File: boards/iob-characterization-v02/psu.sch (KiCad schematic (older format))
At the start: 0 parts

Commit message: Continued work on IOB characterization v0.2 board. On hold until protection network is figured out
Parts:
- added U11, U12: SIP32408, symbol SIP32408
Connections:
- net labels added: VCCO_HI, VCCO_LO
- net labels removed: VCCO
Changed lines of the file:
@@
 encoding utf-8
 Sheet 2 2
-Title ""
-Date ""
-Rev ""
-Comp ""
+Title "STARSHIPRAIDER I/O Characterization"
+Date "2017-05-18"
+Rev "0.2"
+Comp "Andrew Zonenberg"
 Comment1 ""
 Comment2 ""
@@
 I2C to host is 3.3V, shift it to 5V
 Text HLabel 5050 1000 0    60   Output ~ 0
-VCCO
+VCCO_HI
 Text HLabel 5050 1100 0    60   Output ~ 0
 VCLIP_HI
@@
 Text HLabel 5050 1350 0    60   Output ~ 0
 2V5
+Text HLabel 5050 900  0    60   Output ~ 0
+VCCO_LO
+$Comp
+L SIP32408 U11
+U 1 1 591F646E
+P 7100 2250
+F 0 "U11" H 7400 3047 60  0000 C CNN
+F 1 "SIP32408" H 7400 2941 60  0000 C CNN
+F 2 "" H 7100 2250 60  0000 C CNN
+F 3 "" H 7100 2250 60  0000 C CNN
+	1    7100 2250
+	1    0    0    -1
+$EndComp
+$Comp
+L SIP32408 U12
+U 1 1 591F64B0
+P 7100 3300
+F 0 "U12" H 7400 4097 60  0000 C CNN
+F 1 "SIP32408" H 7400 3991 60  0000 C CNN
+F 2 "" H 7100 3300 60  0000 C CNN
+F 3 "" H 7100 3300 60  0000 C CNN
+	1    7100 3300
+	1    0    0    -1
+$EndComp
 $EndSCHEMATC

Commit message: Continued work on iob characterization board
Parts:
- added J2: GREENPAK_DEVKIT_HDR, symbol iob-characterization-v02-rescue:GREENPAK_DEVKIT_HDR
- added R1, R2: R, symbol iob-characterization-v02-rescue:R
- added U1: ISL24021IRT065Z-T7A‎, symbol analog-azonenberg:ISL24021IRT065Z-T7A‎
- U11, U12: value SIP32408 -> SIP32409; symbol SIP32408 -> iob-characterization-v02-rescue:SIP32408
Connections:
- net labels added: VCCO, VCCO_ATTEN, VCCO_IS_HI, VCCO_IS_LO, VCCO_REF
- net labels removed: I2C_SCL, I2C_SDA, VCLIP_HI, VCLIP_LO
- wire segments 0 -> 28
- no-connect marks 0 -> 2
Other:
- note added: "Buffer DAC output to generate VCCO"
- note added: "Greenpak runs at 5V Vdd"
- note added: "Load switches for output power rails"
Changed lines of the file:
@@
-EESchema Schematic File Version 2
-LIBS:conn
-LIBS:device
-LIBS:analog-azonenberg
-LIBS:cmos
-LIBS:cypress-azonenberg
-LIBS:hirose-azonenberg
-LIBS:memory-azonenberg
-LIBS:microchip-azonenberg
-LIBS:osc-azonenberg
-LIBS:passive-azonenberg
-LIBS:power-azonenberg
-LIBS:special-azonenberg
-LIBS:xilinx-azonenberg
+EESchema Schematic File Version 4
 LIBS:iob-characterization-v02-cache
 EELAYER 26 0
@@
 $Descr A4 11693 8268
 encoding utf-8
-Sheet 2 2
+Sheet 2 6
 Title "STARSHIPRAIDER I/O Characterization"
-Date "2017-05-18"
+Date "2018-08-09"
 Rev "0.2"
-Comp "Andrew Zonenberg"
+Comp "Andrew D. Zonenberg"
 Comment1 ""
 Comment2 ""
@@
 Text HLabel 1600 850  0    60   Input ~ 0
 12V0
-Text HLabel 1600 950  0    60   Input ~ 0
+Text HLabel 5300 5350 0    60   Input ~ 0
 5V0
-Text HLabel 1600 1050 0    60   Input ~ 0
+Text HLabel 5300 5450 0    60   Input ~ 0
 GND
-Text HLabel 1600 1400 0    60   Input ~ 0
-I2C_SDA
-Text HLabel 1600 1500 0    60   Input ~ 0
-I2C_SCL
 Text Notes 1400 6650 0    60   ~ 0
 I2C to host is 3.3V, shift it to 5V
-Text HLabel 5050 1000 0    60   Output ~ 0
+Text HLabel 9900 850  2    60   Output ~ 0
 VCCO_HI
-Text HLabel 5050 1100 0    60   Output ~ 0
-VCLIP_HI
-Text HLabel 5050 1200 0    60   Output ~ 0
-VCLIP_LO
 Text HLabel 5050 1350 0    60   Output ~ 0
 2V5
-Text HLabel 5050 900  0    60   Output ~ 0
+Text HLabel 9900 1900 2    60   Output ~ 0
 VCCO_LO
 $Comp
-L SIP32408 U11
+L iob-characterization-v02-rescue:SIP32408 U11
 U 1 1 591F646E
-P 7100 2250
-F 0 "U11" H 7400 3047 60  0000 C CNN
-F 1 "SIP32408" H 7400 2941 60  0000 C CNN
-F 2 "" H 7100 2250 60  0000 C CNN
-F 3 "" H 7100 2250 60  0000 C CNN
-	1    7100 2250
+P 8850 1400
+F 0 "U11" H 9150 2197 60  0000 C CNN
+F 1 "SIP32409" H 9150 2091 60  0000 C CNN
+F 2 "" H 8850 1400 60  0000 C CNN
+F 3 "" H 8850 1400 60  0000 C CNN
+	1    8850 1400
 	1    0    0    -1
 $EndComp
 $Comp
-L SIP32408 U12
+L iob-characterization-v02-rescue:SIP32408 U12
 U 1 1 591F64B0
-P 7100 3300
-F 0 "U12" H 7400 4097 60  0000 C CNN
-F 1 "SIP32408" H 7400 3991 60  0000 C CNN
-F 2 "" H 7100 3300 60  0000 C CNN
-F 3 "" H 7100 3300 60  0000 C CNN
-	1    7100 3300
+P 8850 2450
+F 0 "U12" H 9150 3247 60  0000 C CNN
+F 1 "SIP32409" H 9150 3141 60  0000 C CNN
+F 2 "" H 8850 2450 60  0000 C CNN
+F 3 "" H 8850 2450 60  0000 C CNN
+	1    8850 2450
 	1    0    0    -1
 $EndComp
+Text HLabel 5300 5650 0    50   Input ~ 0
+VCCO_REF
+$Comp
+L iob-characterization-v02-rescue:GREENPAK_DEVKIT_HDR J?
+U 1 1 5B7FF35E
+P 8950 6100
+AR Path="/5B7FF35E" Ref="J?"  Part="1"
+AR Path="/591D3AB5/5B7FF35E" Ref="J2"  Part="1"
+F 0 "J2" H 8950 8250 60  0000 L CNN
+F 1 "GREENPAK_DEVKIT_HDR" H 8950 6050 60  0000 L CNN
+F 2 "" H 8950 6050 60  0001 C CNN
+F 3 "" H 8950 6050 60  0001 C CNN
+	1    8950 6100
+	1    0    0    -1
+$EndComp
+NoConn ~ 8750 4050
+Text Label 8550 4150 2    60   ~ 0
+GND
+Wire Wire Line
+	8550 4150 8750 4150
+NoConn ~ 8750 5450
+$Comp
+L iob-characterization-v02-rescue:R R?
+U 1 1 5B7FF369
+P 9450 3200
+AR Path="/5B7FF369" Ref="R?"  Part="1"
+AR Path="/591D3AB5/5B7FF369" Ref="R1"  Part="1"
+F 0 "R1" V 9350 3200 50  0000 C CNN
+F 1 "R" V 9450 3200 50  0000 C CNN
+F 2 "" V 9380 3200 50  0000 C CNN
+F 3 "" H 9450 3200 50  0000 C CNN
+	1    9450 3200
+	-1   0    0    1
+$EndComp
+$Comp
+L iob-characterization-v02-rescue:R R?
+U 1 1 5B7FF370
+P 9450 3700
+AR Path="/5B7FF370" Ref="R?"  Part="1"
+AR Path="/591D3AB5/5B7FF370" Ref="R2"  Part="1"
+F 0 "R2" V 9350 3700 50  0000 C CNN
+F 1 "R" V 9450 3700 50  0000 C CNN
+F 2 "" V 9380 3700 50  0000 C CNN
+F 3 "" H 9450 3700 50  0000 C CNN
+	1    9450 3700
+	-1   0    0    1
+$EndComp
+Text Label 8550 4750 2    60   ~ 0
+VCCO_ATTEN
+Wire Wire Line
+	8550 4750 8750 4750
+Text Label 9450 3450 2    60   ~ 0
+VCCO_ATTEN
+Wire Wire Line
+	9450 3350 9450 3550
+Text Label 9300 3850 2    60   ~ 0
+GND
+Wire Wire Line
+	9450 3850 9300 3850
+Text Label 9300 3050 2    60   ~ 0
+VCCO
+Wire Wire Line
+	9300 3050 9450 3050
+Text Label 8550 850  2    60   ~ 0
+VCCO
+Wire Wire Line
+	9900 850  9650 850
+Wire Wire Line
+	9900 1900 9650 1900
+Text Label 8550 1900 2    60   ~ 0
+VCCO
+Text Label 8550 1050 2    60   ~ 0
+GND
+Text Label 8550 2100 2    60   ~ 0
+GND
+Wire Wire Line
+	8650 2200 8550 2200
+Wire Wire Line
+	8550 2200 8550 2100
+Wire Wire Line
+	8650 2100 8550 2100
+Wire Wire Line
+	8650 1150 8550 1150
+Wire Wire Line
+	8550 1150 8550 1050
+Wire Wire Line
+	8650 1050 8550 1050
+Wire Wire Line
+	8650 850  8550 850
+Wire Wire Line
+	8550 1350 8650 1350
+Wire Wire Line
+	8550 2400 8650 2400
+Text Notes 8850 2550 0    60   ~ 0
+Load switches for output power rails
+Wire Wire Line
+	8650 1900 8550 1900
+Text Notes 8950 6300 0    50   ~ 0
+Greenpak runs at 5V Vdd
+$Comp
+L analog-azonenberg:ISL24021IRT065Z-T7A‎ U1
+U 1 1 5B8022FF
+P 5550 5850
+F 0 "U1" H 5900 6575 50  0000 C CNN
+F 1 "ISL24021IRT065Z-T7A‎" H 5900 6484 50  0000 C CNN
+F 2 "" H 5550 5850 50  0001 C CNN
+F 3 "" H 5550 5850 50  0001 C CNN
+	1    5550 5850
+	1    0    0    -1
+$EndComp
+Wire Wire Line
+	5300 5450 5450 5450
+Wire Wire Line
+	5450 5350 5300 5350
+Text Label 6650 5650 0    50   ~ 0
+VCCO
+Wire Wire Line
+	6650 5650 6500 5650
+Wire Wire Line
+	5450 5750 5300 5750
+Wire Wire Line
+	5300 5750 5300 5950
+Wire Wire Line
+	5300 5950 6500 5950
+Wire Wire Line
+	6500 5950 6500 5650
+Connection ~ 6500 5650
+Wire Wire Line
+	6500 5650 6350 5650
+Wire Wire Line
+	5300 5650 5450 5650
+Text Notes 5550 6050 0    50   ~ 0
+Buffer DAC output to generate VCCO
+Wire Wire Line
+	8550 4650 8750 4650
+Wire Wire Line
+	8550 4550 8750 4550
+Text HLabel 8550 4550 0    60   Output ~ 0
+VCCO_IS_HI
+Text Label 8550 1350 2    60   ~ 0
+VCCO_IS_HI
+Text Label 8550 2400 2    60   ~ 0
+VCCO_IS_LO
+Text Label 8550 4650 2    60   ~ 0
+VCCO_IS_LO
 $EndSCHEMATC

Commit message: Continued work on IOB characterization platform
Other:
- note removed: "I2C to host is 3.3V, shift it to 5V"
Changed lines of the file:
@@
 Text HLabel 5300 5450 0    60   Input ~ 0
 GND
-Text Notes 1400 6650 0    60   ~ 0
-I2C to host is 3.3V, shift it to 5V
 Text HLabel 9900 850  2    60   Output ~ 0
 VCCO_HI

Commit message: Finished initial schematic of v0.2 IO characterization board. Need to pick component values for protection stage still.
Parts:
- removed J2: GREENPAK_DEVKIT_HDR, symbol iob-characterization-v02-rescue:GREENPAK_DEVKIT_HDR
- removed R1, R2: R, symbol iob-characterization-v02-rescue:R
- added C17, C18, C19: 4.7 uF, symbol device:C
- added D4, D5, D6, D7: RED, symbol device:LED
- added R1, R2: 10K, symbol device:R
- added R17, R18, R19, R20: 470, symbol device:R
- added R21: 50 mR, symbol passive-azonenberg:R-4TERM
- added U18: LDO1117-25, symbol power-azonenberg:LDO1117-XX
- added U19: TCA6424A, symbol special-azonenberg:TCA6424A
- added U20: INA226, symbol special-azonenberg:INA226
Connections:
- net labels added: 3V3, I2C_SCL, I2C_SDA, VCCO_OVERCURRENT, VCCO_OVERVOLT, VCCO_REF_TOOHIGH, VCCO_UNDERVOLT, VSHUNT_HI, VSHUNT_LO
- net labels removed: 12V0, VCCO_ATTEN
- wire segments 28 -> 37
- no-connect marks 2 -> 19
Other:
- note added: "Address = 8'h44"
- note added: "Address = 8'h80"
- note added: "IO buffers have 24 mA drive, with 8 active that's 192 mA.\nTarget 250 mA full scale, 50 mR is 12.5 mV (13.3 bit resolution)"
- note removed: "Greenpak runs at 5V Vdd"
- moved on the sheet: U1

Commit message: Continued work on I/O characterization schematic
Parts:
- C17, C18, C19: footprint (none) -> azonenberg_pcb:EIA_0603_CAP_NOSILK
- R1, R2: footprint (none) -> azonenberg_pcb:EIA_0402_CAP_NOSILK
- R17, R18, R19, R20: footprint (none) -> azonenberg_pcb:EIA_0402_RES_NOSILK
- R21: footprint (none) -> azonenberg_pcb:OHMITE_LVK12
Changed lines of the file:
@@
 Sheet 2 6
 Title "STARSHIPRAIDER I/O Characterization"
-Date "2018-08-10"
+Date "2018-08-13"
 Rev "0.2"
 Comp "Andrew D. Zonenberg"
@@
 F 0 "C19" H 9915 2096 50  0000 L CNN
 F 1 "4.7 uF" H 9915 2005 50  0000 L CNN
-F 2 "" H 9838 1900 50  0001 C CNN
+F 2 "azonenberg_pcb:EIA_0603_CAP_NOSILK" H 9838 1900 50  0001 C CNN
 F 3 "" H 9800 2050 50  0001 C CNN
 	1    9800 2050
@@
 F 0 "C18" H 9915 1046 50  0000 L CNN
 F 1 "4.7 uF" H 9915 955 50  0000 L CNN
-F 2 "" H 9838 850 50  0001 C CNN
+F 2 "azonenberg_pcb:EIA_0603_CAP_NOSILK" H 9838 850 50  0001 C CNN
 F 3 "" H 9800 1000 50  0001 C CNN
 	1    9800 1000
@@
 F 0 "C17" H 8515 5696 50  0000 L CNN
 F 1 "4.7 uF" H 8515 5605 50  0000 L CNN
-F 2 "" H 8438 5500 50  0001 C CNN
+F 2 "azonenberg_pcb:EIA_0603_CAP_NOSILK" H 8438 5500 50  0001 C CNN
 F 3 "" H 8400 5650 50  0001 C CNN
 	1    8400 5650
@@
 F 0 "R1" V 3400 1700 50  0000 C CNN
 F 1 "10K" V 3450 1550 50  0000 C CNN
-F 2 "" V 3380 1550 50  0001 C CNN
+F 2 "azonenberg_pcb:EIA_0402_CAP_NOSILK" V 3380 1550 50  0001 C CNN
 F 3 "" H 3450 1550 50  0001 C CNN
 	1    3450 1550
@@
 F 0 "R2" V 3400 1900 50  0000 C CNN
 F 1 "10K" V 3450 1750 50  0000 C CNN
-F 2 "" V 3380 1750 50  0001 C CNN
+F 2 "azonenberg_pcb:EIA_0402_CAP_NOSILK" V 3380 1750 50  0001 C CNN
 F 3 "" H 3450 1750 50  0001 C CNN
 	1    3450 1750
@@
 F 0 "R17" V 5850 1200 50  0000 C CNN
 F 1 "470" V 5900 1050 50  0000 C CNN
-F 2 "" V 5830 1050 50  0001 C CNN
+F 2 "azonenberg_pcb:EIA_0402_RES_NOSILK" V 5830 1050 50  0001 C CNN
 F 3 "" H 5900 1050 50  0001 C CNN
 	1    5900 1050
@@
 F 0 "R18" V 5850 1550 50  0000 C CNN
 F 1 "470" V 5900 1400 50  0000 C CNN
-F 2 "" V 5830 1400 50  0001 C CNN
+F 2 "azonenberg_pcb:EIA_0402_RES_NOSILK" V 5830 1400 50  0001 C CNN
 F 3 "" H 5900 1400 50  0001 C CNN
 	1    5900 1400
@@
 F 0 "R19" V 5850 1950 50  0000 C CNN
 F 1 "470" V 5900 1800 50  0000 C CNN
-F 2 "" V 5830 1800 50  0001 C CNN
+F 2 "azonenberg_pcb:EIA_0402_RES_NOSILK" V 5830 1800 50  0001 C CNN
 F 3 "" H 5900 1800 50  0001 C CNN
 	1    5900 1800
@@
 F 0 "R20" V 5850 2350 50  0000 C CNN
 F 1 "470" V 5900 2200 50  0000 C CNN
-F 2 "" V 5830 2200 50  0001 C CNN
+F 2 "azonenberg_pcb:EIA_0402_RES_NOSILK" V 5830 2200 50  0001 C CNN
 F 3 "" H 5900 2200 50  0001 C CNN
 	1    5900 2200
@@
 F 0 "R21" V 8864 5750 50  0000 C CNN
 F 1 "50 mR" V 8955 5750 50  0000 C CNN
-F 2 "" H 9150 5750 60  0001 C CNN
+F 2 "azonenberg_pcb:OHMITE_LVK12" H 9150 5750 60  0001 C CNN
 F 3 "" H 9150 5750 60  0000 C CNN
 	1    9150 5750

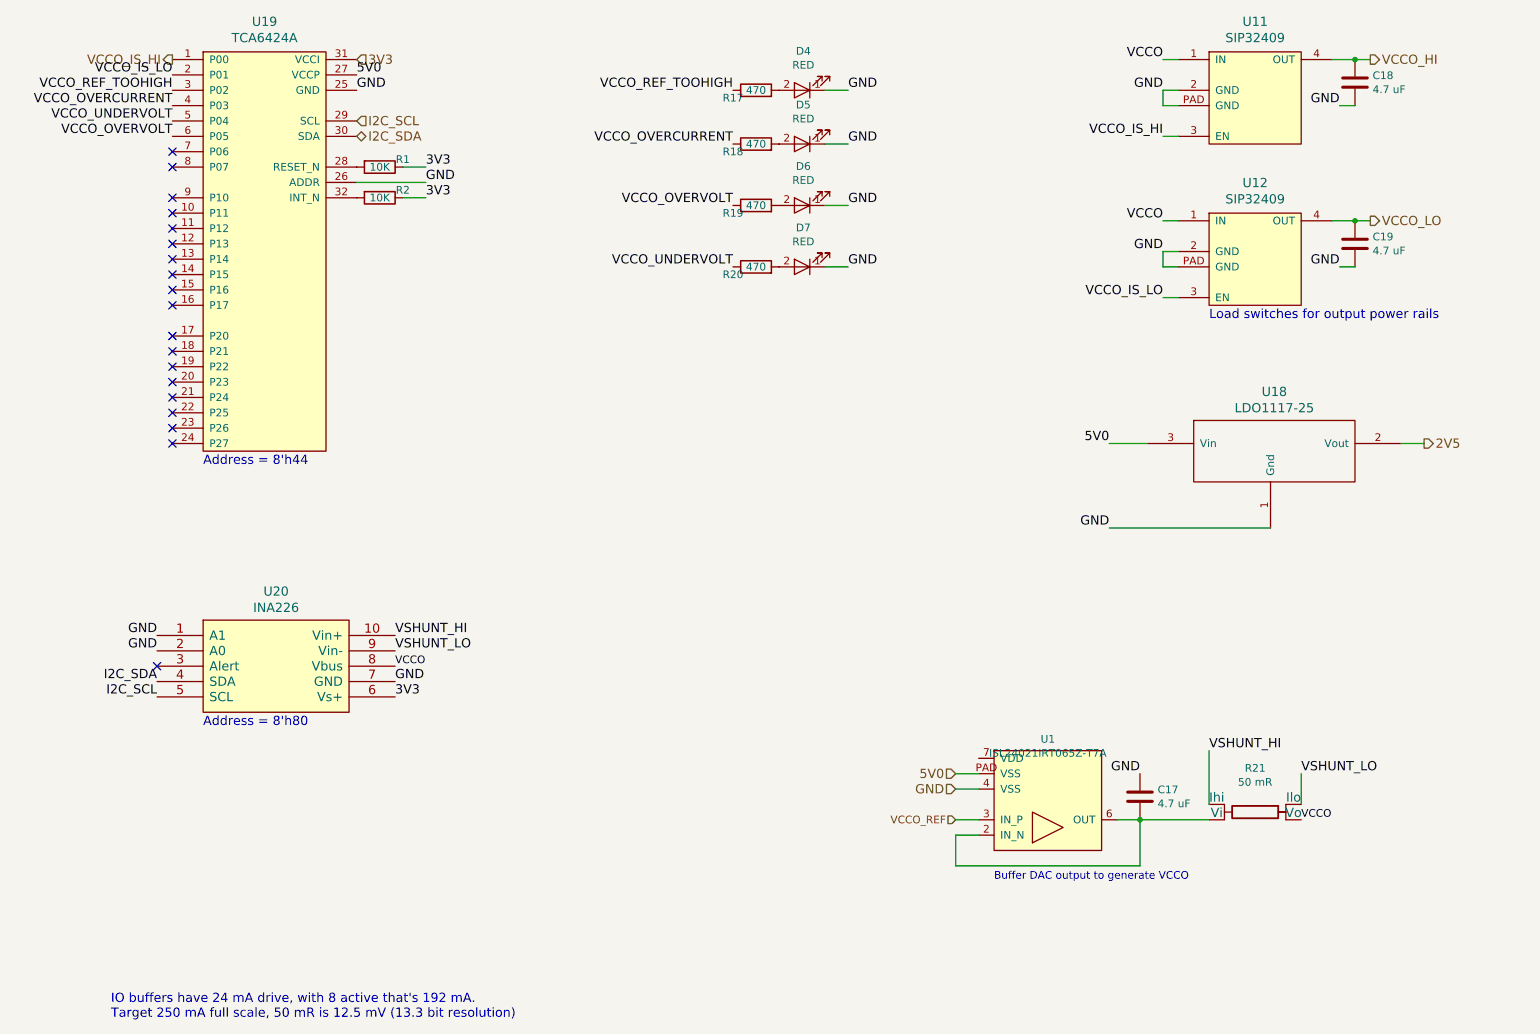
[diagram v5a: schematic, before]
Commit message: Continued initial routing of IOB characterization board
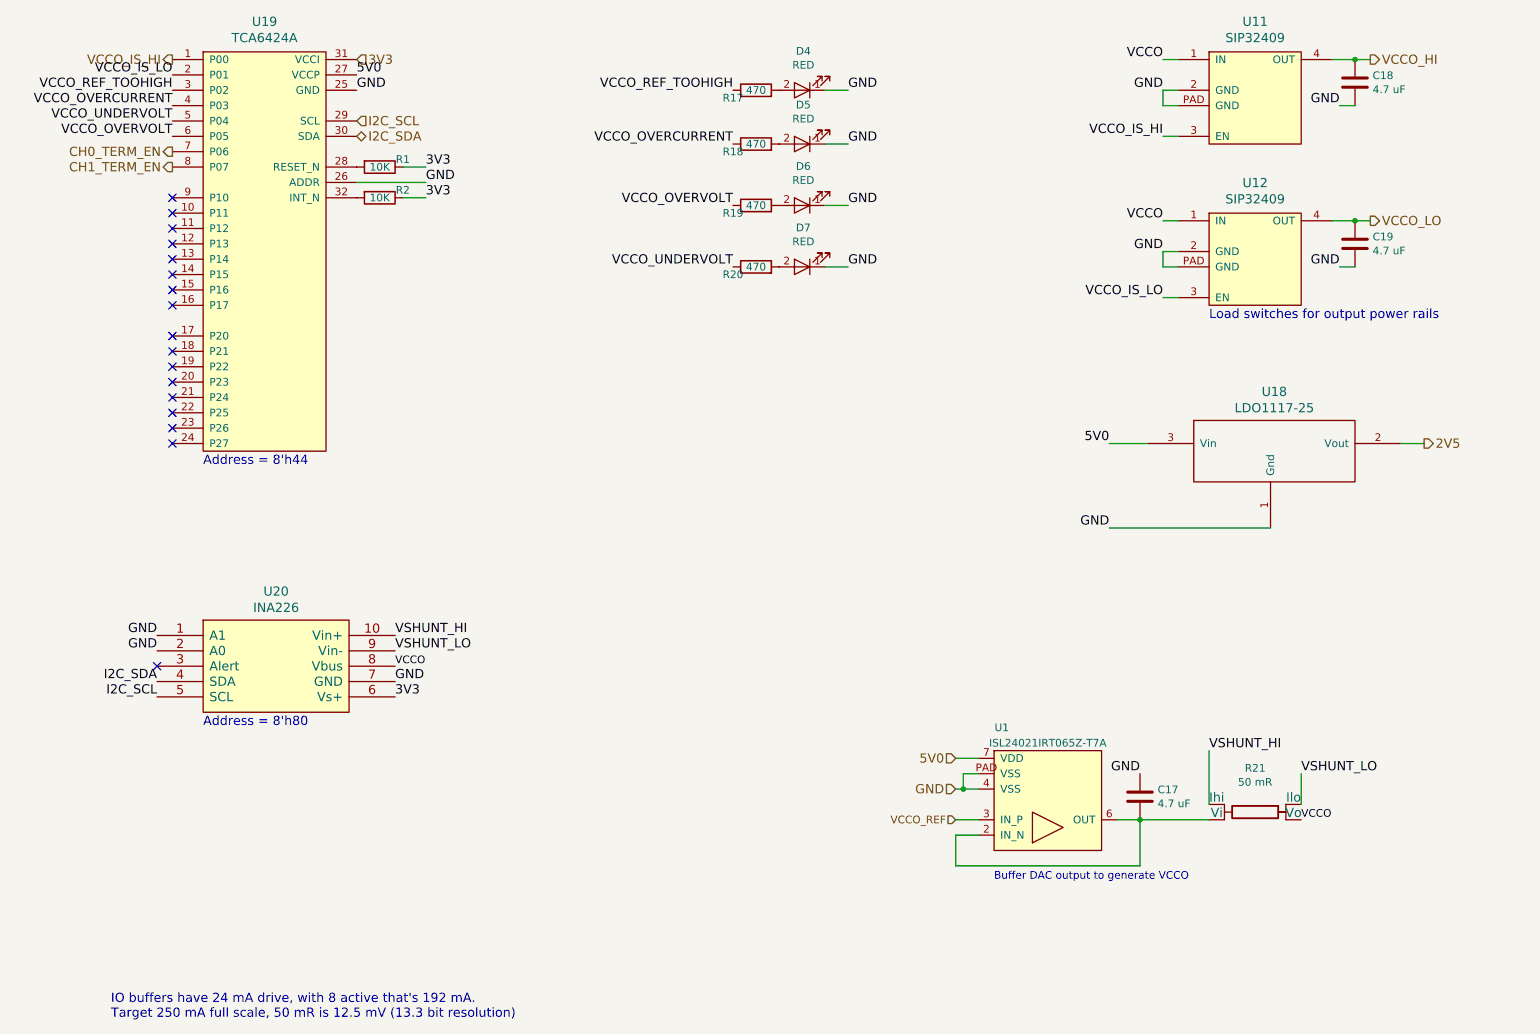
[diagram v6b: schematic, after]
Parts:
- D4, D5, D6, D7: footprint (none) -> azonenberg_pcb:EIA_0603_LED
- U1: footprint (none) -> azonenberg_pcb:DFN_8_0.65MM_3x3MM
- U11, U12: footprint (none) -> azonenberg_pcb:DFN_4_0.5MM_1.6x1.2MM
- U18: footprint (none) -> azonenberg_pcb:SOT223-4
- U19: footprint (none) -> azonenberg_pcb:QFN_32_0.5MM_5x5MM
- U20: footprint (none) -> azonenberg_pcb:SOP_10_0.5MM_3MM
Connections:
- net 5V0: now also U1.7 (VDD); no longer U1.PAD (VSS)
- net GND: now also U1.PAD (VSS)
- net CH0_TERM_EN: now reaches U19.7 (P06)
- net CH1_TERM_EN: now reaches U19.8 (P07)
- no-connect marks 19 -> 17
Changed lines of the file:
@@
 Sheet 2 6
 Title "STARSHIPRAIDER I/O Characterization"
-Date "2018-08-13"
+Date "2018-08-15"
 Rev "0.2"
 Comp "Andrew D. Zonenberg"
@@
 Comment4 ""
 $EndDescr
-Text HLabel 7200 5500 0    60   Input ~ 0
+Text HLabel 7200 5400 0    60   Input ~ 0
 5V0
 Text HLabel 7200 5600 0    60   Input ~ 0
@@
 F 0 "U11" H 9150 2197 60  0000 C CNN
 F 1 "SIP32409" H 9150 2091 60  0000 C CNN
-F 2 "" H 8850 1400 60  0001 C CNN
+F 2 "azonenberg_pcb:DFN_4_0.5MM_1.6x1.2MM" H 8850 1400 60  0001 C CNN
 F 3 "" H 8850 1400 60  0000 C CNN
 	1    8850 1400
@@
 F 0 "U12" H 9150 3247 60  0000 C CNN
 F 1 "SIP32409" H 9150 3141 60  0000 C CNN
-F 2 "" H 8850 2450 60  0001 C CNN
+F 2 "azonenberg_pcb:DFN_4_0.5MM_1.6x1.2MM" H 8850 2450 60  0001 C CNN
 F 3 "" H 8850 2450 60  0000 C CNN
 	1    8850 2450
@@
 U 1 1 5B8022FF
 P 7450 6000
-F 0 "U1" H 7800 6725 50  0000 C CNN
-F 1 "ISL24021IRT065Z-T7A‎" H 7800 6634 50  0000 C CNN
-F 2 "" H 7450 6000 50  0001 C CNN
+F 0 "U1" H 7500 6800 50  0000 C CNN
+F 1 "ISL24021IRT065Z-T7A‎" H 7800 6700 50  0000 C CNN
+F 2 "azonenberg_pcb:DFN_8_0.65MM_3x3MM" H 7450 6000 50  0001 C CNN
 F 3 "" H 7450 6000 50  0001 C CNN
 	1    7450 6000
@@
 $EndComp
 Wire Wire Line
-	7200 5600 7350 5600
-Wire Wire Line
-	7350 5500 7200 5500
+	7200 5600 7250 5600
+Wire Wire Line
+	7350 5400 7200 5400
 Text Label 9450 5800 0    50   ~ 0
 VCCO
@@
 F 0 "U18" H 9275 3487 60  0000 C CNN
 F 1 "LDO1117-25" H 9275 3381 60  0000 C CNN
-F 2 "" H 9200 3250 60  0001 C CNN
+F 2 "azonenberg_pcb:SOT223-4" H 9200 3250 60  0001 C CNN
 F 3 "" H 9200 3250 60  0000 C CNN
 	1    9200 3250
@@
 F 0 "U19" H 2700 6197 60  0000 C CNN
 F 1 "TCA6424A" H 2700 6091 60  0000 C CNN
-F 2 "" H 2300 3400 60  0001 C CNN
+F 2 "azonenberg_pcb:QFN_32_0.5MM_5x5MM" H 2300 3400 60  0001 C CNN
 F 3 "" H 2300 3400 60  0000 C CNN
 	1    2300 3400
@@
 F 0 "D4" H 6192 795 50  0000 C CNN
 F 1 "RED" H 6192 886 50  0000 C CNN
-F 2 "" H 6200 1050 50  0001 C CNN
+F 2 "azonenberg_pcb:EIA_0603_LED" H 6200 1050 50  0001 C CNN
 F 3 "" H 6200 1050 50  0001 C CNN
 	1    6200 1050
@@
 NoConn ~ 2100 1850
 NoConn ~ 2100 1750
-NoConn ~ 2100 1450
-NoConn ~ 2100 1550
 $Comp
 L special-azonenberg:INA226 U20
@@
 F 0 "U20" H 2775 5287 60  0000 C CNN
 F 1 "INA226" H 2775 5181 60  0000 C CNN
-F 2 "" H 2800 4800 60  0001 C CNN
+F 2 "azonenberg_pcb:SOP_10_0.5MM_3MM" H 2800 4800 60  0001 C CNN
 F 3 "" H 2800 4800 60  0000 C CNN
 	1    2800 4800
@@
 F 0 "D5" H 6192 1145 50  0000 C CNN
 F 1 "RED" H 6192 1236 50  0000 C CNN
-F 2 "" H 6200 1400 50  0001 C CNN
+F 2 "azonenberg_pcb:EIA_0603_LED" H 6200 1400 50  0001 C CNN
 F 3 "" H 6200 1400 50  0001 C CNN
 	1    6200 1400
@@
 F 0 "D6" H 6192 1545 50  0000 C CNN
 F 1 "RED" H 6192 1636 50  0000 C CNN
-F 2 "" H 6200 1800 50  0001 C CNN
+F 2 "azonenberg_pcb:EIA_0603_LED" H 6200 1800 50  0001 C CNN
 F 3 "" H 6200 1800 50  0001 C CNN
 	1    6200 1800
@@
 F 0 "D7" H 6192 1945 50  0000 C CNN
 F 1 "RED" H 6192 2036 50  0000 C CNN
-F 2 "" H 6200 2200 50  0001 C CNN
+F 2 "azonenberg_pcb:EIA_0603_LED" H 6200 2200 50  0001 C CNN
 F 3 "" H 6200 2200 50  0001 C CNN
 	1    6200 2200
@@
 Text Notes 2300 5200 0    60   ~ 0
 Address = 8'h80
+Wire Wire Line
+	7350 5500 7250 5500
+Wire Wire Line
+	7250 5500 7250 5600
+Connection ~ 7250 5600
+Wire Wire Line
+	7250 5600 7350 5600
+Text HLabel 2100 1450 0    60   Output ~ 0
+CH0_TERM_EN
+Text HLabel 2100 1550 0    60   Output ~ 0
+CH1_TERM_EN
 $EndSCHEMATC
